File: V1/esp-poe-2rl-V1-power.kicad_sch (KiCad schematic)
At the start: 32 parts

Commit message: Layout development
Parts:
- U?: footprint Tales:SOIC-8-1EP_3.9x4.9mm_P1.27mm_EP2.95x4.9mm_Mask2.71x3.4mm_ThermalVias -> Package_SO:SOIC-8-1EP_3.9x4.9mm_P1.27mm_EP2.95x4.9mm_Mask2.71x3.4mm_ThermalVias
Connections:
- net PoE-: now also U?.9 (PPAD)
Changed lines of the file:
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@@
   (junction (at 64.77 60.96) (diameter 0) (color 0 0 0 0)
+  )
+  (junction (at 123.19 54.61) (diameter 0) (color 0 0 0 0)
   )
   (junction (at 142.24 43.18) (diameter 0) (color 0 0 0 0)
@@
     (stroke (width 0) (type default))
   )
+  (wire (pts (xy 123.19 54.61) (xy 120.65 54.61))
+    (stroke (width 0) (type default))
+  )
   (wire (pts (xy 90.17 163.83) (xy 106.68 163.83))
     (stroke (width 0) (type default))
@@
     (stroke (width 0) (type default))
   )
-  (wire (pts (xy 100.33 60.96) (xy 120.65 60.96))
+  (wire (pts (xy 100.33 60.96) (xy 123.19 60.96))
     (stroke (width 0) (type default))
   )
@@
     (stroke (width 0) (type default))
   )
+  (wire (pts (xy 120.65 54.61) (xy 120.65 52.07))
+    (stroke (width 0) (type default))
+  )
   (wire (pts (xy 63.5 166.37) (xy 63.5 168.91))
     (stroke (width 0) (type default))
@@
     (stroke (width 0) (type default))
   )
+  (wire (pts (xy 123.19 52.07) (xy 123.19 54.61))
+    (stroke (width 0) (type default))
+  )
   (wire (pts (xy 133.35 148.59) (xy 114.3 148.59))
     (stroke (width 0) (type default))
@@
     (stroke (width 0) (type default))
   )
-  (wire (pts (xy 120.65 60.96) (xy 120.65 52.07))
+  (wire (pts (xy 123.19 60.96) (xy 123.19 54.61))
     (stroke (width 0) (type default))
   )
@@
   )
   (symbol (lib_id "Tales:TPS2376") (at 120.65 41.91 0) (unit 1)
-    (in_bom yes) (on_board yes) (dnp no) (fields_autoplaced)
-    (property "Reference" "U?" (at 122.6059 52.07 0)
-      (effects (font (size 1.27 1.27)) (justify left))
-    )
-    (property "Value" "TPS2376DDAR-H" (at 122.6059 54.61 0)
-      (effects (font (size 1.27 1.27)) (justify left))
-    )
-    (property "Footprint" "Tales:SOIC-8-1EP_3.9x4.9mm_P1.27mm_EP2.95x4.9mm_Mask2.71x3.4mm_ThermalVias" (at 120.65 62.23 0)
+    (in_bom yes) (on_board yes) (dnp no)
+    (property "Reference" "U?" (at 124.46 52.07 0)
+      (effects (font (size 1.27 1.27)) (justify left))
+    )
+    (property "Value" "TPS2376DDAR-H" (at 124.46 54.61 0)
+      (effects (font (size 1.27 1.27)) (justify left))
+    )
+    (property "Footprint" "Package_SO:SOIC-8-1EP_3.9x4.9mm_P1.27mm_EP2.95x4.9mm_Mask2.71x3.4mm_ThermalVias" (at 120.65 62.23 0)
       (effects (font (size 1.27 1.27)) hide)
     )
@@
       (effects (font (size 1.27 1.27)) hide)
     )
-    (property "LCSC Part #" "C544899" (at 122.6059 57.15 0)
+    (property "LCSC Part #" "C544899" (at 124.46 57.15 0)
       (effects (font (size 1.27 1.27)) (justify left))
     )
@@
     (pin "7")
     (pin "8")
-    (instances
-      (project "esp-poe-2rl-V1"
+    (pin "9")
+    (instances
+      (project "esp-poe-2rl-V1"

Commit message: Layout optimization
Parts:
- L?: footprint Tales:L_3x3_H1.5 -> Tales:L_3x3_h1.5
- L?: footprint Tales:L_12x12mm_H6mm -> Tales:L_12x12mm_h6mm
- U?: footprint Package_SO:SOIC-8-1EP_3.9x4.9mm_P1.27mm_EP2.95x4.9mm_Mask2.71x3.4mm_ThermalVias -> Tales:SOIC-8-1EP_3.9x4.9mm_P1.27mm_EP2.95x4.9mm_Mask2.71x3.4mm_ThermalVias
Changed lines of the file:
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@@
       (effects (font (size 1.27 1.27)))
     )
-    (property "Footprint" "Tales:L_3x3_H1.5" (at 96.52 148.59 0)
+    (property "Footprint" "Tales:L_3x3_h1.5" (at 96.52 148.59 0)
       (effects (font (size 1.27 1.27)) hide)
     )
@@
       (effects (font (size 1.27 1.27)))
     )
-    (property "Footprint" "Tales:L_12x12mm_H6mm" (at 95.25 96.52 0)
+    (property "Footprint" "Tales:L_12x12mm_h6mm" (at 95.25 96.52 0)
       (effects (font (size 1.27 1.27)) hide)
     )
@@
       (effects (font (size 1.27 1.27)) (justify left))
     )
-    (property "Footprint" "Package_SO:SOIC-8-1EP_3.9x4.9mm_P1.27mm_EP2.95x4.9mm_Mask2.71x3.4mm_ThermalVias" (at 120.65 62.23 0)
-      (effects (font (size 1.27 1.27)) hide)
-    )
+    (property "Footprint" "Tales:SOIC-8-1EP_3.9x4.9mm_P1.27mm_EP2.95x4.9mm_Mask2.71x3.4mm_ThermalVias" (at 120.65 62.23 0)
+      (effects (font (size 1.27 1.27)) hide)
+    )

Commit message: PCB shrinking process
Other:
- note removed: "OK"
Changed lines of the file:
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@@
     (effects (font (size 1.5 1.5)) (justify left bottom))
-  )
-  (text "OK" (at 16.51 44.45 0)
-    (effects (font (size 5 5)) (justify left bottom))
   )
   (text "R_{TX1}" (at 119.38 102.87 0)
@@
     (effects (font (size 2.54 2.54)) (justify left bottom))
   )
-  (text "OK" (at 16.51 97.79 0)
-    (effects (font (size 5 5)) (justify left bottom))
-  )
-  (text "OK" (at 16.51 160.02 0)
-    (effects (font (size 5 5)) (justify left bottom))
-  )
   (text "MPS LOAD" (at 160.02 45.72 0)

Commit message: Migrating layout to 4 layers
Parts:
- L?: footprint Tales:L_3x3_h1.5 -> Tales:L_3x3_H1.5
- L?: footprint Tales:L_12x12mm_h6mm -> Tales:L_12x12mm_H6mm
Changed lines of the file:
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@@
       (effects (font (size 1.27 1.27)))
     )
-    (property "Footprint" "Tales:L_3x3_h1.5" (at 96.52 148.59 0)
+    (property "Footprint" "Tales:L_3x3_H1.5" (at 96.52 148.59 0)
       (effects (font (size 1.27 1.27)) hide)
     )
@@
       (effects (font (size 1.27 1.27)))
     )
-    (property "Footprint" "Tales:L_12x12mm_h6mm" (at 95.25 96.52 0)
-      (effects (font (size 1.27 1.27)) hide)
-    )
+    (property "Footprint" "Tales:L_12x12mm_H6mm" (at 95.25 96.52 0)
+      (effects (font (size 1.27 1.27)) hide)
+    )

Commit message: Last touches
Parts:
- L?: footprint Tales:L_3x3_H1.5 -> Tales:L_3x3_h1.5
- L?: footprint Tales:L_12x12mm_H6mm -> Tales:L_12x12mm_h6mm
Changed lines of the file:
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@@
       (effects (font (size 1.27 1.27)))
     )
-    (property "Footprint" "Tales:L_3x3_H1.5" (at 96.52 148.59 0)
+    (property "Footprint" "Tales:L_3x3_h1.5" (at 96.52 148.59 0)
       (effects (font (size 1.27 1.27)) hide)
     )
@@
       (effects (font (size 1.27 1.27)))
     )
-    (property "Footprint" "Tales:L_12x12mm_H6mm" (at 95.25 96.52 0)
-      (effects (font (size 1.27 1.27)) hide)
-    )
+    (property "Footprint" "Tales:L_12x12mm_h6mm" (at 95.25 96.52 0)
+      (effects (font (size 1.27 1.27)) hide)
+    )

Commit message: Tweaks to components
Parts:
- C? (x2), R?: Case 1206/3216 -> (none); Package (none) -> 1206/3216
- C?: Case 0805/2012 -> (none); Package (none) -> 0805/2012; Technology Ceramic X7R -> Ceramix X7R
- C?, R? (x2): Case 0805/2012 -> (none); Package (none) -> 0805/2012
- C?, R? (x4): Case 0402/1005 -> (none); Package (none) -> 0402/1005
- C? (x2): Case D8xL10.5mm -> (none); Package (none) -> D8xL10.5mm
- C? (x2), R? (x5): Case 0603/1608 -> (none); Package (none) -> 0603/1608
- D? (x3): Case SMA -> (none); Package (none) -> SMA
- D?: Case SMA/DO-214AC -> (none); Package (none) -> SMA/DO-214AC
- D?: Case 0603 -> (none); Package (none) -> 0603
- L?: Case 3x3 -> (none); Package (none) -> 3x3
- L?: Case 12x12 -> (none); Package (none) -> 12x12
- R?: Case 2512/6332 -> (none); Package (none) -> 2512/6332
- U?: Case SO-8 -> (none); Package (none) -> SO-8
- U?: Case SOIC-8 -> (none); Package (none) -> SOIC-8
- U?: Case SOT-23-5 -> (none); Package (none) -> SOT-23-5

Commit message: Update image
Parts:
- L?: footprint Tales:L_3x3_h1.5 -> Tales:L_3x3mm_h1.5mm
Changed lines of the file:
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@@
       (effects (font (size 1.27 1.27)))
     )
-    (property "Footprint" "Tales:L_3x3_h1.5" (at 96.52 148.59 0)
+    (property "Footprint" "Tales:L_3x3mm_h1.5mm" (at 96.52 148.59 0)
       (effects (font (size 1.27 1.27)) hide)
     )

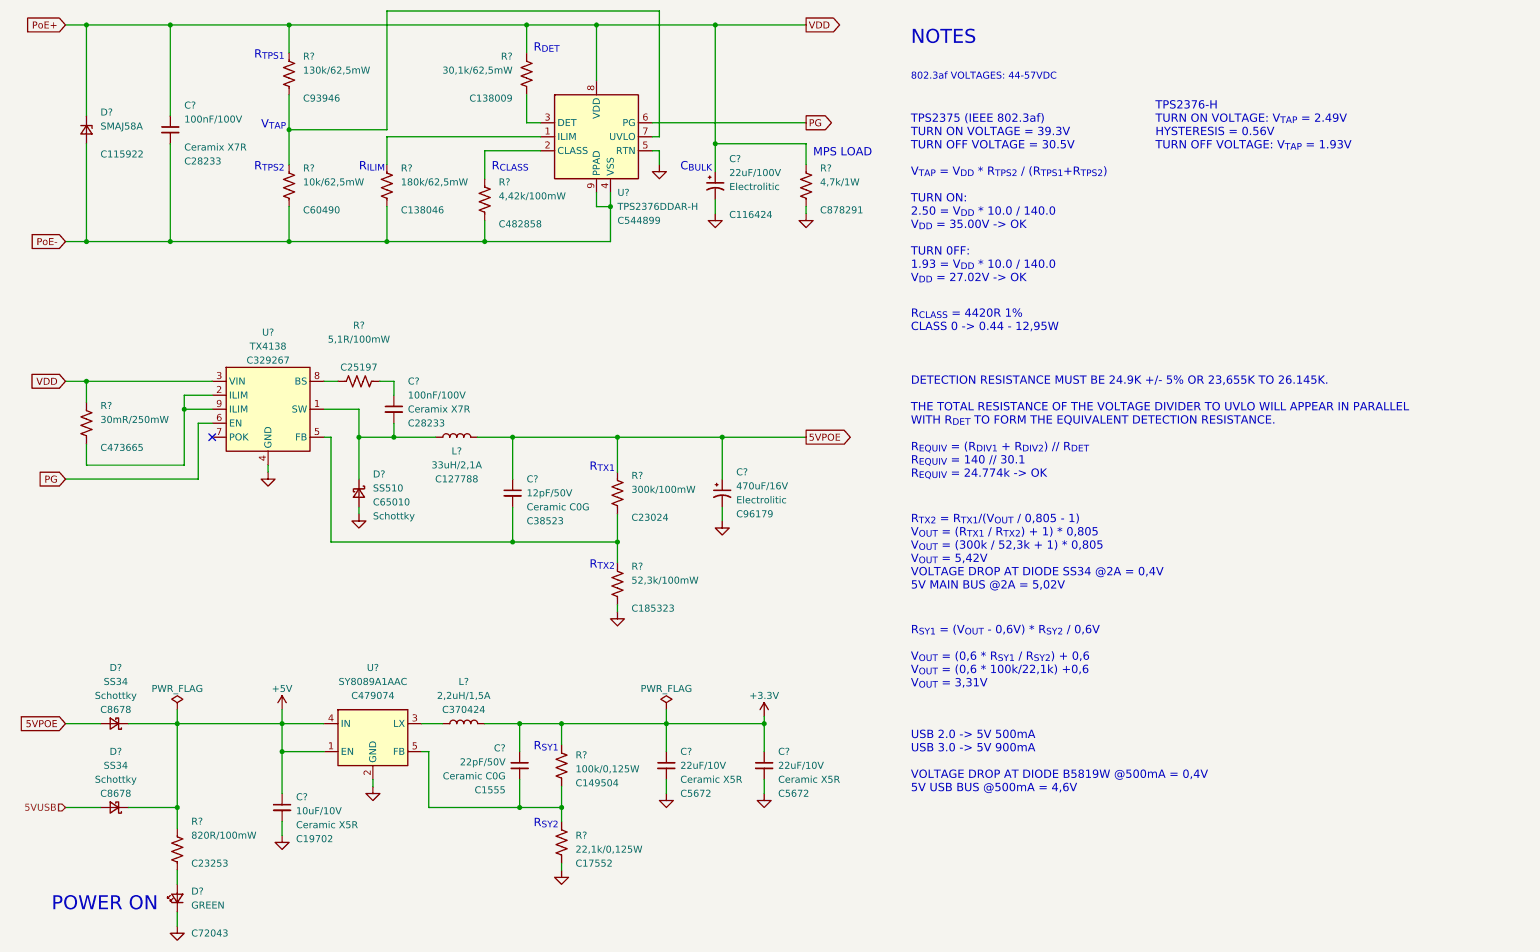
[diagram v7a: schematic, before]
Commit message: Update to Kicad V8
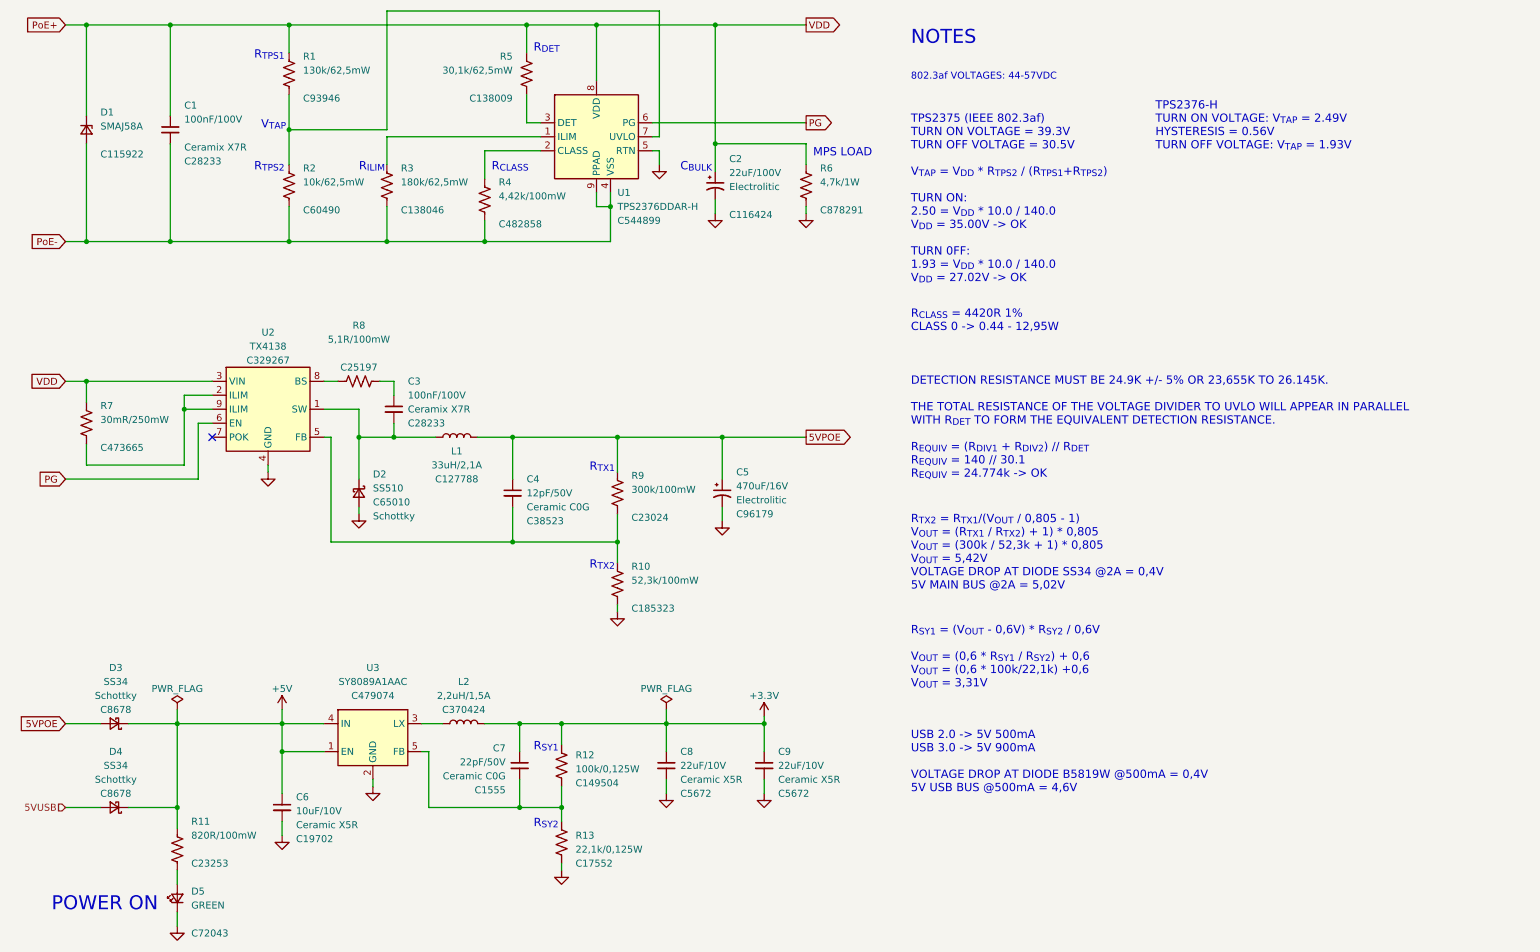
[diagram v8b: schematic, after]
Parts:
- gave numbers to parts that had none: 32
